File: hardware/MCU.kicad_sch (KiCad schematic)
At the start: 22 parts, among them Q1 2N2219, Q2 2N2219, SW2 GPIO_N_RST, SW3 SW_SYS-PWR, SW4 GPIO_HW_ADDR_SEL, U3 SX1509BIULTRT

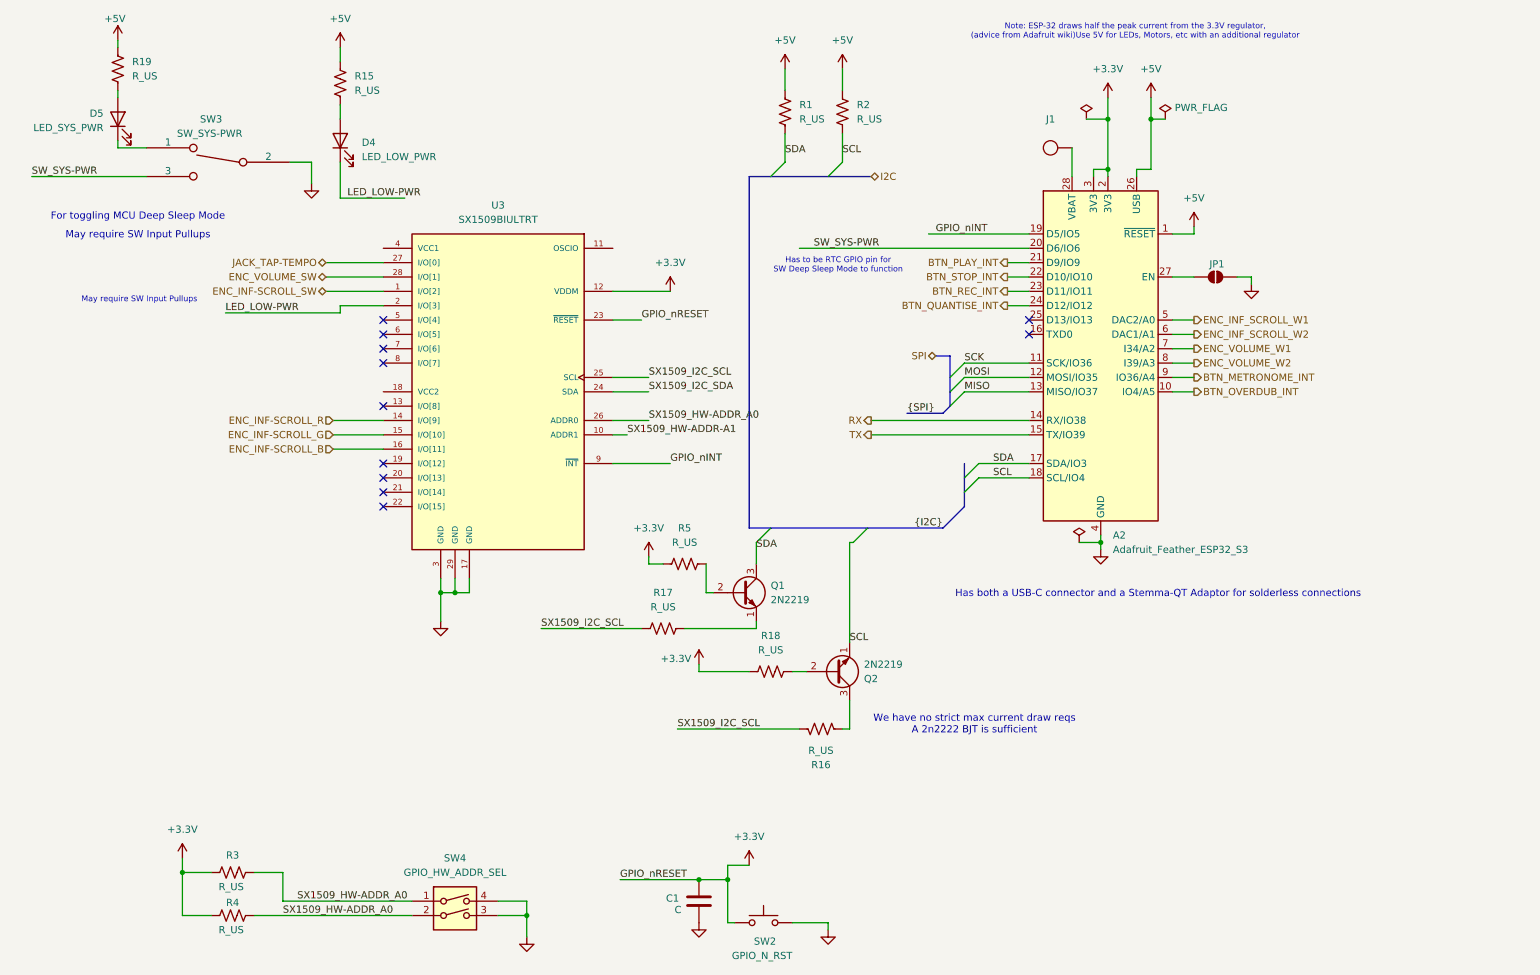
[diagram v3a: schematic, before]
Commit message: feat [HWE]: Add to SX1509 Circuitry
We adapt the SX1509 of the design to the design used in the sparkfun SX1509 Breakout Board https://cdn.sparkfun.com/assets/learn_tutorials/4/3/4/sx1509-breakout-schematic.pdf
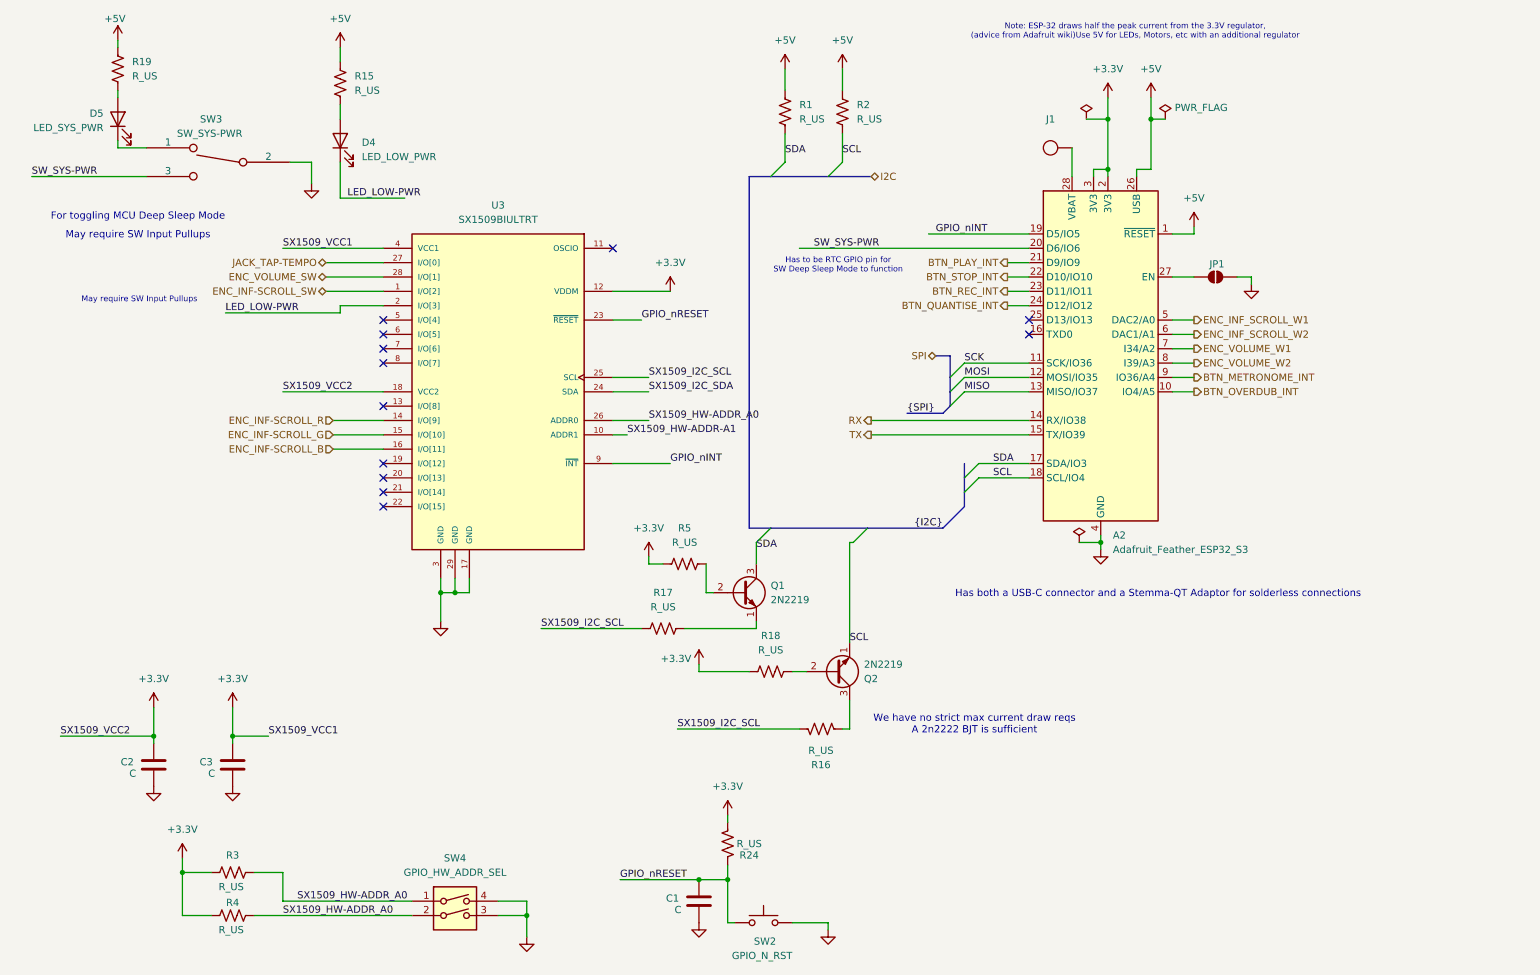
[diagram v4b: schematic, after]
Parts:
- added C2, C3: C, symbol Device:C
- added R24: R_US, symbol Device:R_US
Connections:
- net +3.3V: now also U3.18 (VCC2), U3.4 (VCC1), C2.1, C3.1, R24.2; no longer C1.1, SW2.1, U3.23 (~{RESET})
- net GND: now also C2.2, C3.2
- new net GPIO_nRESET: C1.1, R24.1, SW2.1, U3.23 (~{RESET})
- no-connect marks 11 -> 12

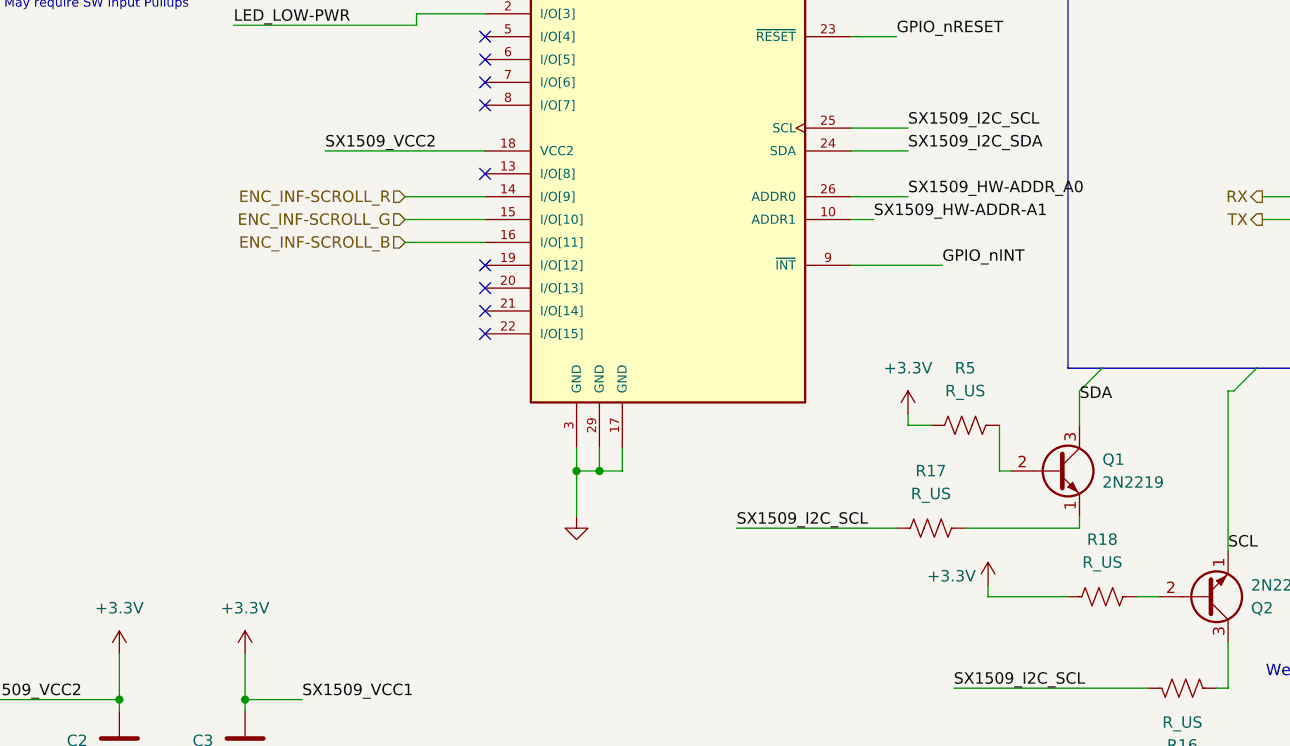
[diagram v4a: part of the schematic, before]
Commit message: fix [HWE]: Moved Inf Scroll ARGB pins on SX1509
Shifted the pins of the R, G and B pins of the infinite scroll encoder from pins 9 - 11 on the SX1509, to pins 8 - 10
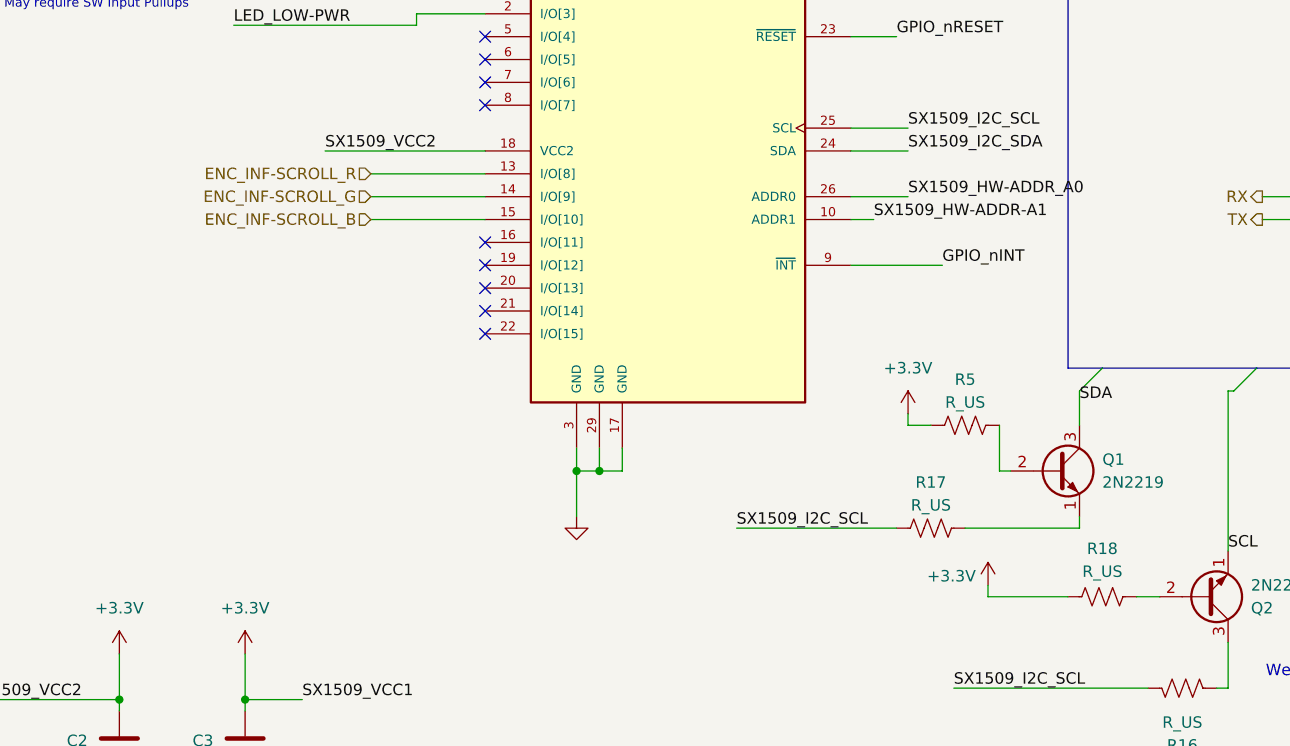
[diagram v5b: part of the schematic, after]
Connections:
- net ENC_INF-SCROLL_B: now also U3.15 (I/O[10]); no longer U3.16 (I/O[11])
- net ENC_INF-SCROLL_G: now also U3.14 (I/O[9]); no longer U3.15 (I/O[10])
- net ENC_INF-SCROLL_R: now also U3.13 (I/O[8]); no longer U3.14 (I/O[9])
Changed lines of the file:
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@@
 	)
 	(no_connect
+		(at 78.74 91.44)
+	)
+	(no_connect
 		(at 78.74 71.12)
 	)
@@
 	)
 	(no_connect
-		(at 78.74 83.82)
-	)
-	(no_connect
 		(at 78.74 101.6)
 	)
@@
 	(wire
 		(pts
+			(xy 66.04 88.9) (xy 78.74 88.9)
+		)
+		(stroke
+			(width 0)
+			(type default)
+		)
+	)
+	(wire
+		(pts
 			(xy 218.44 73.66) (xy 222.25 73.66)
 		)
@@
 	(wire
 		(pts
-			(xy 69.85 91.44) (xy 78.74 91.44)
-		)
-		(stroke
-			(width 0)
-			(type default)
-		)
-	)
-	(wire
-		(pts
 			(xy 50.8 67.31) (xy 71.12 67.31)
 		)
@@
 	(wire
 		(pts
+			(xy 66.04 83.82) (xy 78.74 83.82)
+		)
+		(stroke
+			(width 0)
+			(type default)
+		)
+	)
+	(wire
+		(pts
 			(xy 60.96 81.28) (xy 78.74 81.28)
 		)
@@
 	(wire
 		(pts
-			(xy 69.85 88.9) (xy 78.74 88.9)
-		)
-		(stroke
-			(width 0)
-			(type default)
-		)
-	)
-	(wire
-		(pts
 			(xy 201.93 107.95) (xy 205.74 107.95)
 		)
@@
 	(wire
 		(pts
+			(xy 66.04 86.36) (xy 78.74 86.36)
+		)
+		(stroke
+			(width 0)
+			(type default)
+		)
+	)
+	(wire
+		(pts
 			(xy 55.88 173.99) (xy 83.82 173.99)
 		)
@@
 	(wire
 		(pts
-			(xy 69.85 86.36) (xy 78.74 86.36)
-		)
-		(stroke
-			(width 0)
-			(type default)
-		)
-	)
-	(wire
-		(pts
 			(xy 132.08 123.19) (xy 144.78 123.19)
 		)
@@
 	(hierarchical_label "ENC_INF-SCROLL_B"
 		(shape input)
-		(at 69.85 91.44 180)
+		(at 66.04 88.9 180)
 		(effects
 			(font
@@
 	(hierarchical_label "ENC_INF-SCROLL_G"
 		(shape input)
-		(at 69.85 88.9 180)
+		(at 66.04 86.36 180)
 		(effects
 			(font
@@
 	(hierarchical_label "ENC_INF-SCROLL_R"
 		(shape input)
-		(at 69.85 86.36 180)
+		(at 66.04 83.82 180)
 		(effects
 			(font
@@
 		(on_board yes)
 		(dnp no)
-		(fields_autoplaced yes)
 		(property "Reference" "R17"
-			(at 128.27 116.84 90)
+			(at 128.27 118.11 90)
 			(effects
 				(font
@@
 		)
 		(property "Value" "R_US"
-			(at 128.27 119.38 90)
+			(at 128.27 120.65 90)
 			(effects
 				(font
@@
 		(on_board yes)
 		(dnp no)
-		(fields_autoplaced yes)
 		(property "Reference" "R18"
-			(at 147.32 124.46 90)
+			(at 147.32 125.476 90)
 			(effects
 				(font
@@
 		)
 		(property "Value" "R_US"
-			(at 147.32 127 90)
+			(at 147.32 128.016 90)
 			(effects
 				(font
@@
 		(on_board yes)
 		(dnp no)
-		(fields_autoplaced yes)
 		(property "Reference" "R5"
-			(at 132.08 105.41 90)
+			(at 132.08 106.68 90)
 			(effects
 				(font
@@
 		)
 		(property "Value" "R_US"
-			(at 132.08 107.95 90)
+			(at 132.08 109.22 90)
 			(effects
 				(font

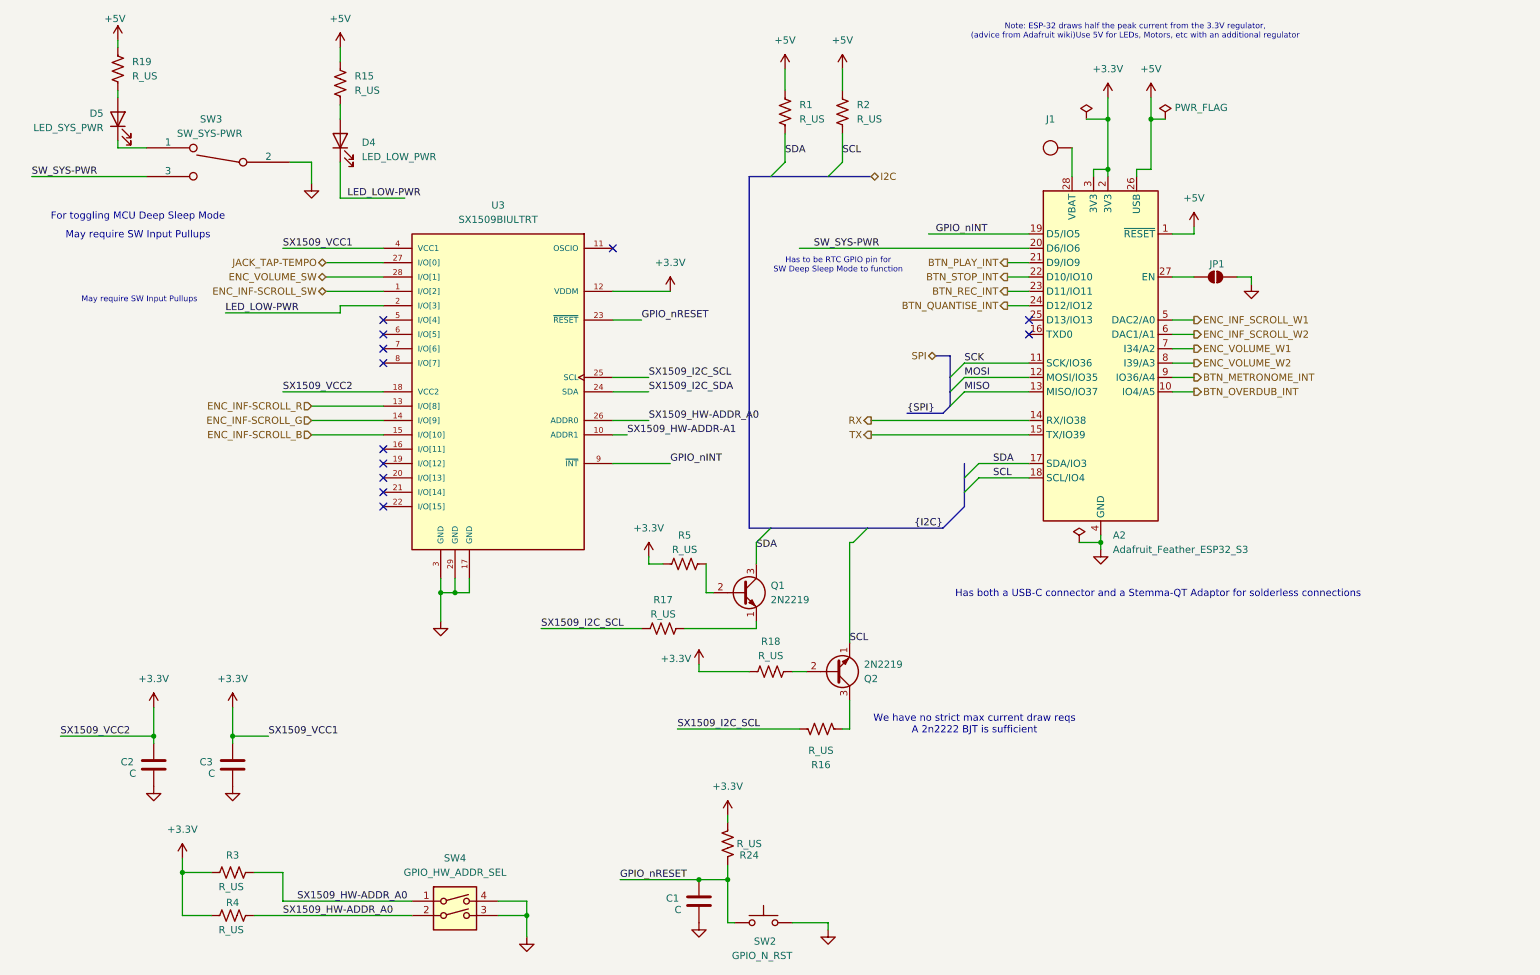
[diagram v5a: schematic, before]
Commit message: misc [HWE]: Clarified SYS_PWR functionality
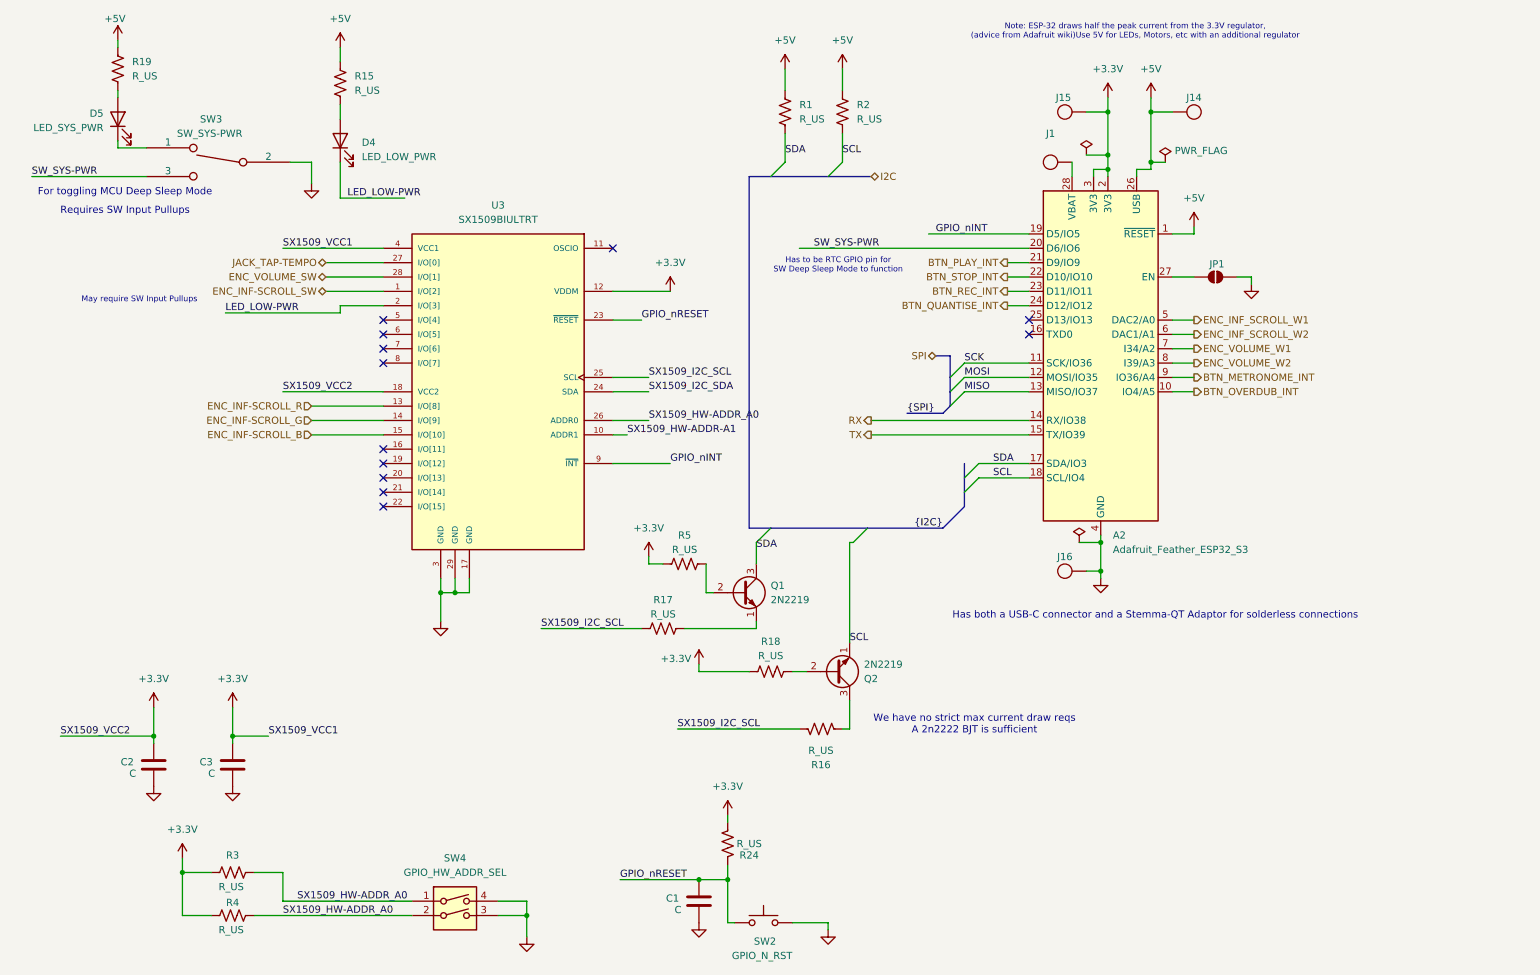
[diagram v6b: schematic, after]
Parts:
- added J14, J15, J16: ~, 4ms_Connector:CAPSENSE_PAD, symbol 4ms_Connector:CAPSENSE_PAD
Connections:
- net +3.3V: now also J15.1 (CS)
- net +5V: now also J14.1 (CS)
- net GND: now also J16.1 (CS)
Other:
- note added: "Requires SW Input Pullups"
- moved on the sheet: J1
